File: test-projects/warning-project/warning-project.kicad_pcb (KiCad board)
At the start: 2 copper layers, 14 x 9 mm, 3 parts, among them J1 Conn_01x02

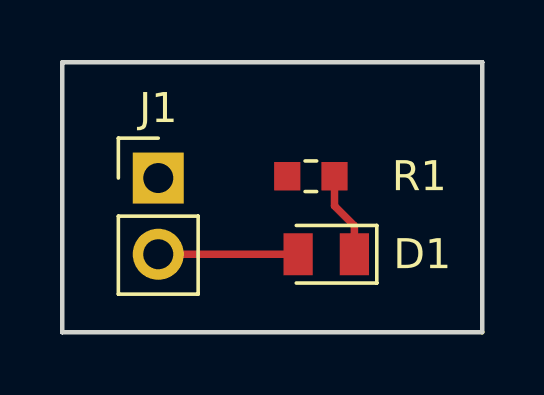
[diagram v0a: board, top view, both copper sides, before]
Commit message: Add UI automation for PCBNew DRC
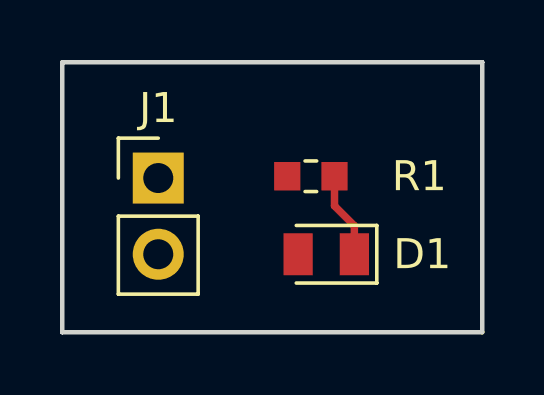
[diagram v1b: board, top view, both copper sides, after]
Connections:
- R1 pad 2: GND -> (no net)
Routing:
- net VCC: track 4.66 -> 0.00 mm
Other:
- board text added: "Pad 2 of J1 and pad 2 of D1 are not connected. We expect an "unconnected" DRC message."
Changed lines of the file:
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@@
-(kicad_pcb (version 4) (host pcbnew 4.0.7)
+(kicad_pcb (version 20171130) (host pcbnew "(5.0.1-3-g963ef8bb5)")
   (general
-    (links 3)
-    (no_connects 0)
-    (area 138.924999 101.924999 153.075001 111.075001)
     (thickness 1.6)
-    (drawings 4)
-    (tracks 4)
+    (drawings 5)
+    (tracks 3)
     (zones 0)
     (modules 3)
@@
     (pad_drill 0.762)
     (pad_to_mask_clearance 0.2)
+    (solder_mask_min_width 0.25)
     (aux_axis_origin 0 0)
     (visible_elements FFFFFF7F)
@@
       (layerselection 0x00030_80000001)
       (usegerberextensions false)
+      (usegerberattributes false)
+      (usegerberadvancedattributes false)
+      (creategerberjobfile false)
       (excludeedgelayer true)
       (linewidth 0.050000)
@@
       (hpglpennumber 1)
       (hpglpenspeed 20)
-      (hpglpendiameter 15)
-      (hpglpenoverlay 2)
+      (hpglpendiameter 15.000000)
       (psnegative false)
       (psa4output false)
@@
     (pad 1 smd rect (at -0.7875 0 180) (size 0.875 0.95) (layers F.Cu F.Paste F.Mask)
       (net 1 "Net-(D1-Pad1)"))
-    (pad 2 smd rect (at 0.7875 0 180) (size 0.875 0.95) (layers F.Cu F.Paste F.Mask)
-      (net 3 GND))
+    (pad 2 smd rect (at 0.7875 0 180) (size 0.875 0.95) (layers F.Cu F.Paste F.Mask))
     (model ${KISYS3DMOD}/Resistor_SMD.3dshapes/R_0603_1608Metric.wrl
       (at (xyz 0 0 0))
@@
       (rotate (xyz 0 0 0))
     )
+  )
+  (gr_text "Pad 2 of J1 and pad 2 of D1 are not connected.\nWe expect an \"unconnected\" DRC message." (at 147 112.6) (layer Dwgs.User)
+    (effects (font (size 0.5 0.5) (thickness 0.1)))
   )
   (gr_line (start 139 111) (end 139 102) (layer Edge.Cuts) (width 0.15))
@@
   (segment (start 148.7375 107.45) (end 148.075 106.7875) (width 0.25) (layer F.Cu) (net 1))
   (segment (start 148.075 106.7875) (end 148.075 105.8) (width 0.25) (layer F.Cu) (net 1))
-  (segment (start 142.2 108.4) (end 146.8625 108.4) (width 0.25) (layer F.Cu) (net 2))
   (zone (net 3) (net_name GND) (layer F.Cu) (hatch edge 0.508)
     (connect_pads (clearance 0.508))

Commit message: Update test projects to KiCad 5
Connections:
- R1 pad 2: (no net) -> Net-(R1-Pad2)
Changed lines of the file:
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@@
-(kicad_pcb (version 20171130) (host pcbnew "(5.0.1-3-g963ef8bb5)")
+(kicad_pcb (version 20171130) (host pcbnew 5.0.1-33cea8e~67~ubuntu18.04.1)
   (general
     (thickness 1.6)
@@
     (zones 0)
     (modules 3)
-    (nets 4)
+    (nets 5)
   )
   (page A4)
@@
   (net 2 VCC)
   (net 3 GND)
+  (net 4 "Net-(R1-Pad2)")
   (net_class Default "This is the default net class."
     (clearance 0.2)
@@
     (add_net GND)
     (add_net "Net-(D1-Pad1)")
+    (add_net "Net-(R1-Pad2)")
     (add_net VCC)
   )
@@
     (pad 1 smd rect (at -0.7875 0 180) (size 0.875 0.95) (layers F.Cu F.Paste F.Mask)
       (net 1 "Net-(D1-Pad1)"))
-    (pad 2 smd rect (at 0.7875 0 180) (size 0.875 0.95) (layers F.Cu F.Paste F.Mask))
+    (pad 2 smd rect (at 0.7875 0 180) (size 0.875 0.95) (layers F.Cu F.Paste F.Mask)
+      (net 4 "Net-(R1-Pad2)"))
     (model ${KISYS3DMOD}/Resistor_SMD.3dshapes/R_0603_1608Metric.wrl
       (at (xyz 0 0 0))
